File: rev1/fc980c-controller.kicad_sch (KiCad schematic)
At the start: 31 parts, among them J1 SWD, J2 USB, J3 KEYBOARD, SW1 BOOT0, U1 XC6206P332MR, U2 STM32F401CBUx, U3 USBLC6-2SC6, U5 PCA9306DC, Y1 8MHz C_l 20pF

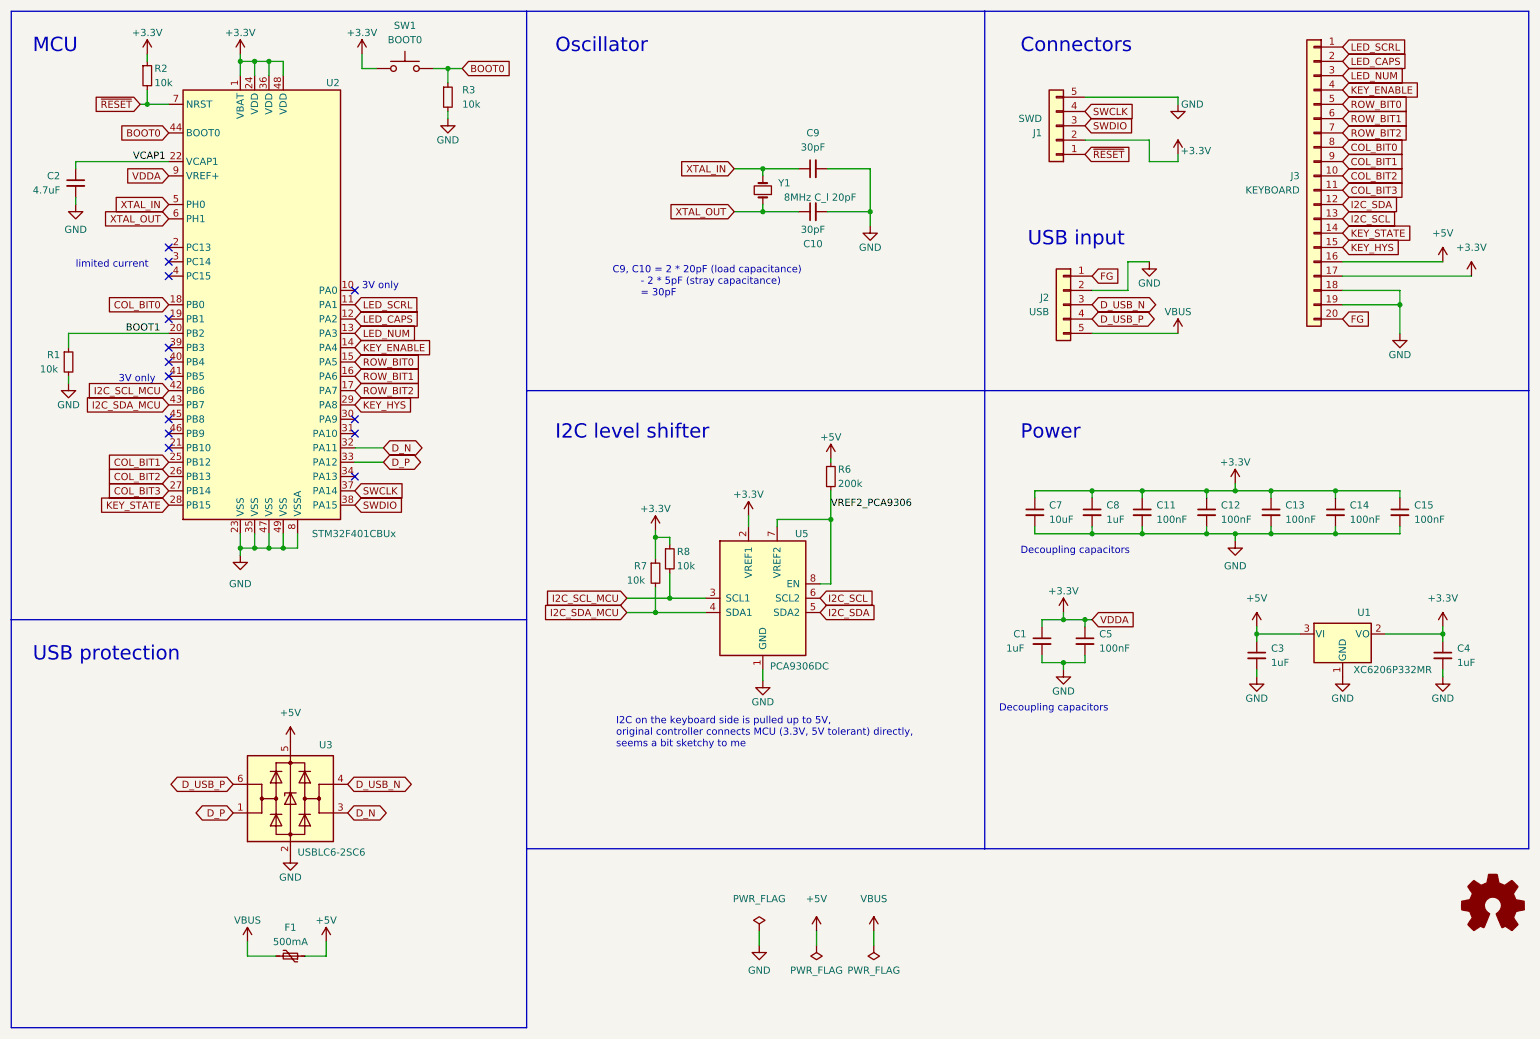
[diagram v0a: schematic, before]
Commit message: rev1: Add EEPROM
This should alleviate needing to use MCU flash for EEPROM emulation.

Also recalculate crystal load capacitor values using guidance from the
MCU datasheet.
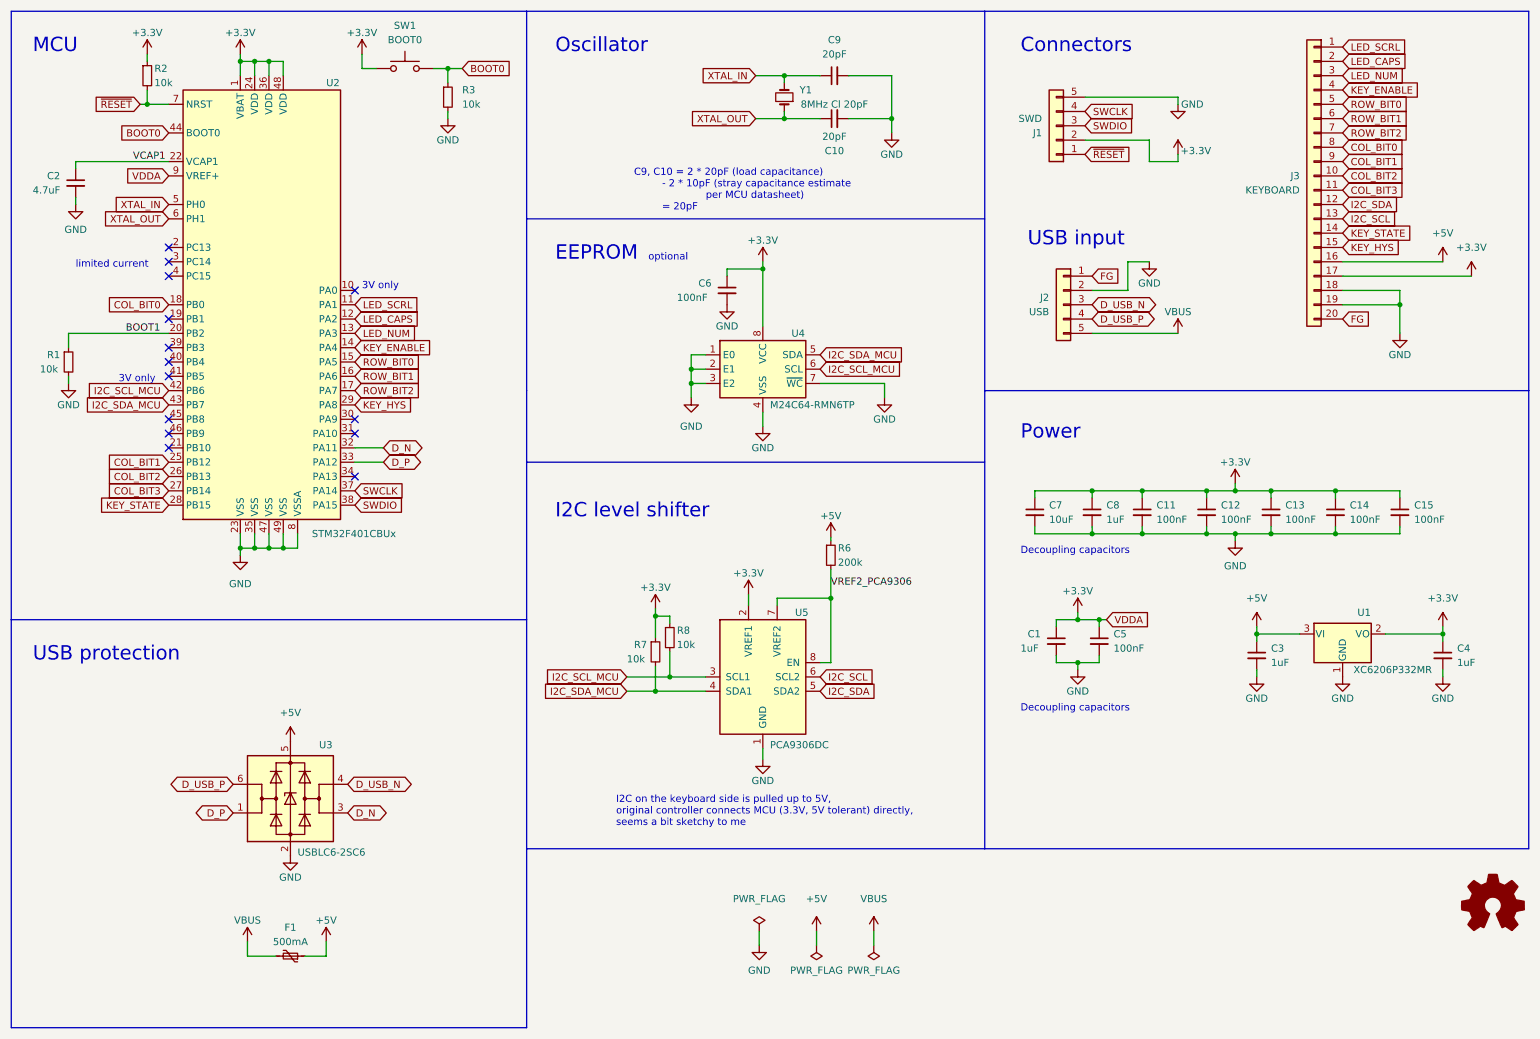
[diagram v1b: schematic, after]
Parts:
- added C6: 100nF, Resistor_SMD:R_0402_1005Metric, symbol Device:C_Small
- added U4: M24C64-RMN6TP, Package_SO:SOIC-8_3.9x4.9mm_P1.27mm, symbol Memory_EEPROM:M24C02-RMN
- C10, C9: value 30pF -> 20pF
- Y1: value 8MHz C_l 20pF -> 8MHz Cl 20pF
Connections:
- net +3.3V: now also C6.1, U4.8 (VCC)
- net GND: now also C6.2, U4.1 (E0), U4.2 (E1), U4.3 (E2), U4.4 (VSS), U4.7 (~{WC})
- net I2C_SCL_MCU: now also U4.6 (SCL)
- net I2C_SDA_MCU: now also U4.5 (SDA)
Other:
- note added: "C9, C10 = 2 * 20pF (load capacitance) - 2 * 10pF (stray capacitance estimate per MCU datasheet) = 20pF"
- note added: "EEPROM"
- note added: "optional"
- note removed: "C9, C10 = 2 * 20pF (load capacitance) - 2 * 5pF (stray capacitance) = 30pF"
- moved on the sheet: C1, C10, C5, C9, R6, R7, R8, U5, Y1

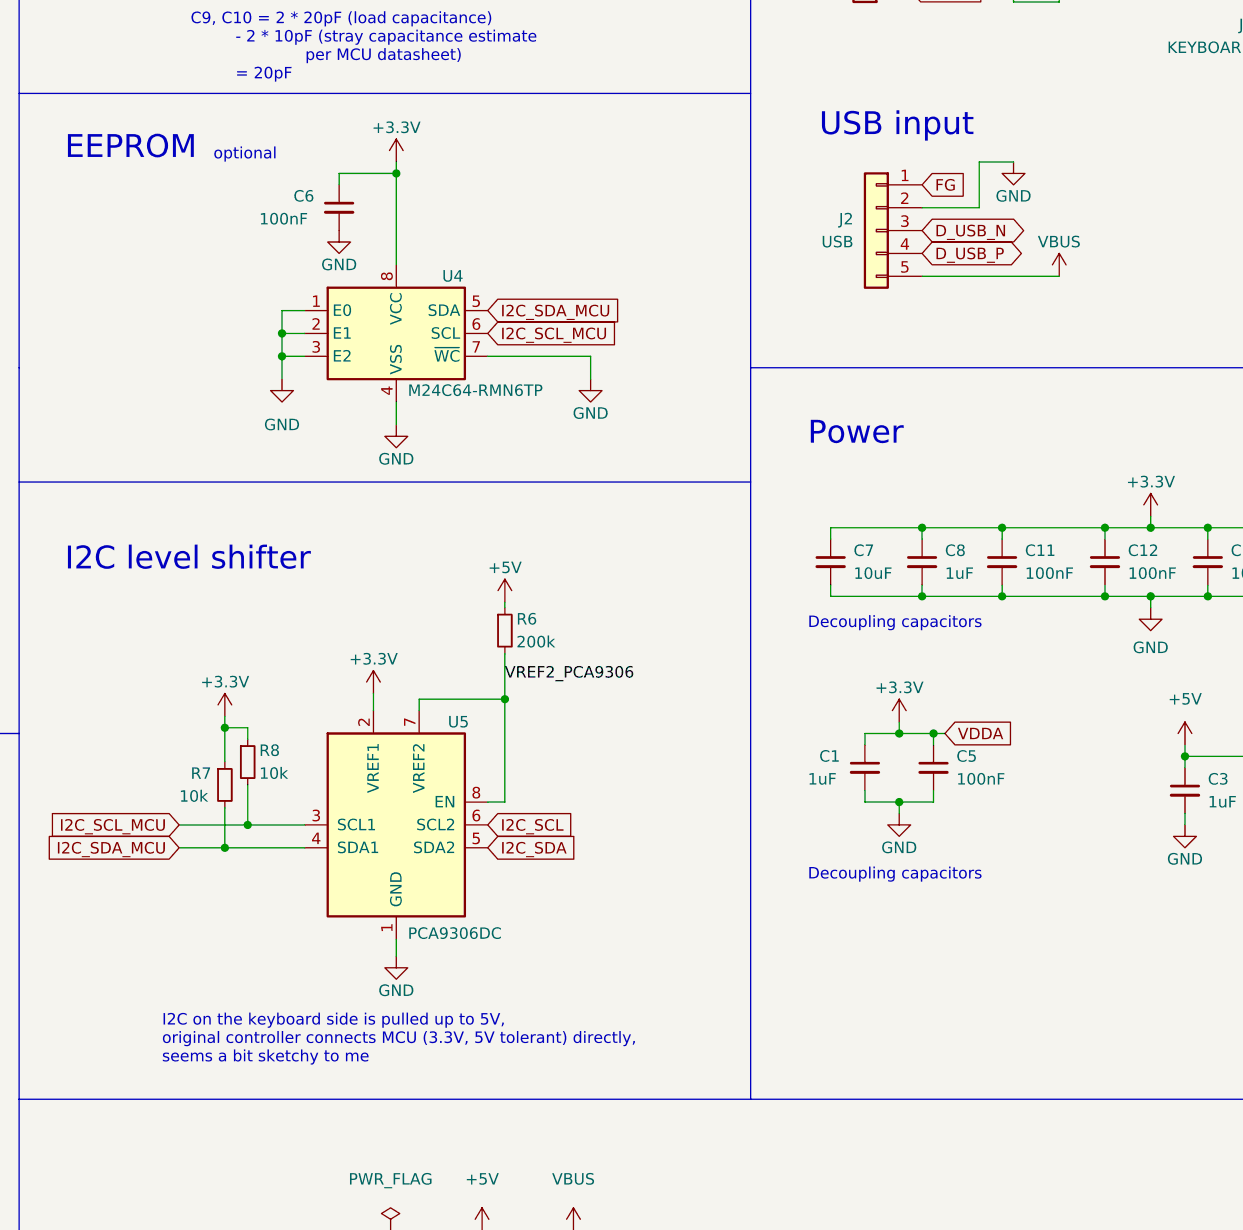
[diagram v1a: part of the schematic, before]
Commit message: rev1: Minor tweaks before first production run
Most notably change to a capacitor footprint rather than resistor
footprint for C6.

Small via tweaks.

Adjust component rotations reviewing JLC SMTA preview. (still waiting on
JLC review at this point)
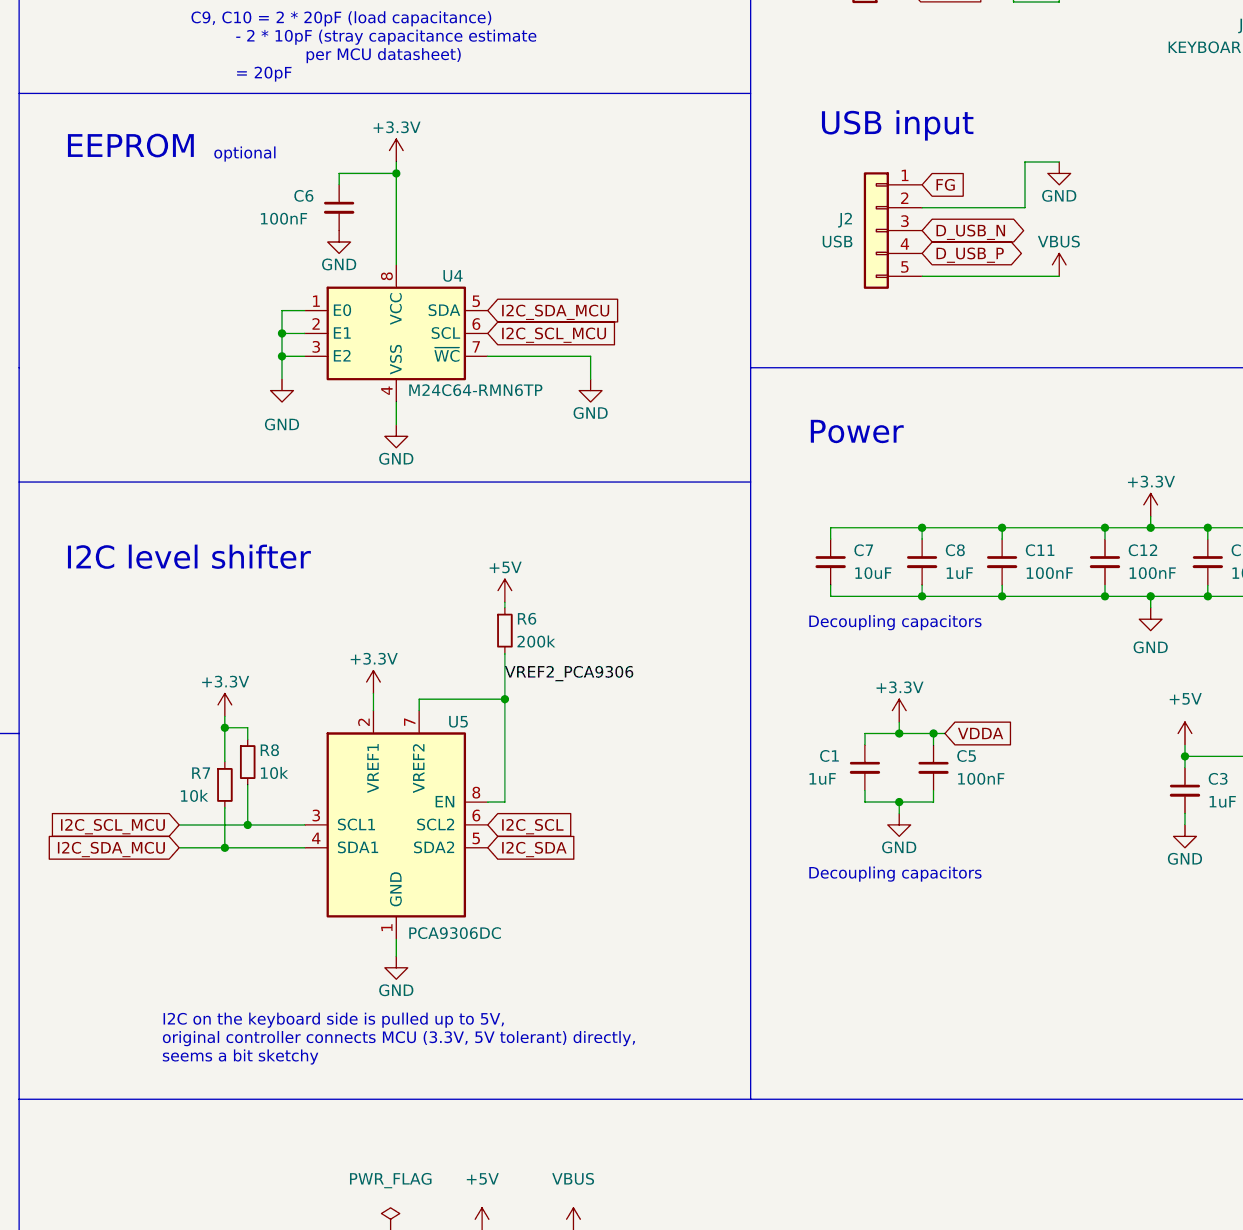
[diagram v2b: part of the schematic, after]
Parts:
- C6: footprint Resistor_SMD:R_0402_1005Metric -> Capacitor_SMD:C_0402_1005Metric
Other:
- note added: "I2C on the keyboard side is pulled up to 5V, original controller connects MCU (3.3V, 5V tolerant) directly, seems a bit sketchy"
- note removed: "I2C on the keyboard side is pulled up to 5V, original controller connects MCU (3.3V, 5V tolerant) directly, seems a bit sketchy to me"
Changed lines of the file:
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@@
     (stroke (width 0) (type default) (color 0 0 0 0))
   )
-  (wire (pts (xy 212.09 59.69) (xy 215.9 59.69))
+  (wire (pts (xy 217.17 59.69) (xy 220.98 59.69))
     (stroke (width 0) (type default) (color 0 0 0 0))
   )
@@
     (stroke (width 0) (type default) (color 0 0 0 0))
   )
-  (wire (pts (xy 205.74 64.77) (xy 212.09 64.77))
+  (wire (pts (xy 205.74 64.77) (xy 217.17 64.77))
     (stroke (width 0) (type default) (color 0 0 0 0))
   )
@@
     (stroke (width 0) (type default) (color 0 0 0 0))
   )
-  (wire (pts (xy 212.09 64.77) (xy 212.09 59.69))
+  (wire (pts (xy 217.17 64.77) (xy 217.17 59.69))
     (stroke (width 0) (type default) (color 0 0 0 0))
   )
@@
     (effects (font (size 2.54 2.54)) (justify left bottom))
   )
-  (text "I2C on the keyboard side is pulled up to 5V,\noriginal controller connects MCU (3.3V, 5V tolerant) directly,\nseems a bit sketchy to me\n"
+  (text "I2C on the keyboard side is pulled up to 5V,\noriginal controller connects MCU (3.3V, 5V tolerant) directly,\nseems a bit sketchy\n"
     (at 121.285 160.02 0)
     (effects (font (size 1.27 1.27)) (justify left bottom))
@@
       (effects (font (size 1.27 1.27)) (justify left))
     )
-    (property "Footprint" "Resistor_SMD:R_0402_1005Metric" (id 2) (at 140.97 64.77 0)
+    (property "Footprint" "Capacitor_SMD:C_0402_1005Metric" (id 2) (at 140.97 64.77 0)
       (effects (font (size 1.27 1.27)) hide)
     )
@@
     (pin "2")
   )
-  (symbol (lib_id "power:GND") (at 215.9 59.69 0) (unit 1)
-    (in_bom yes) (on_board yes)
-    (property "Reference" "#PWR017" (id 0) (at 215.9 66.04 0)
-      (effects (font (size 1.27 1.27)) hide)
-    )
-    (property "Value" "GND" (id 1) (at 215.9 63.5 0))
-    (property "Footprint" "" (id 2) (at 215.9 59.69 0)
-      (effects (font (size 1.27 1.27)) hide)
-    )
-    (property "Datasheet" "" (id 3) (at 215.9 59.69 0)
+  (symbol (lib_id "power:GND") (at 220.98 59.69 0) (unit 1)
+    (in_bom yes) (on_board yes)
+    (property "Reference" "#PWR017" (id 0) (at 220.98 66.04 0)
+      (effects (font (size 1.27 1.27)) hide)
+    )
+    (property "Value" "GND" (id 1) (at 220.98 63.5 0))
+    (property "Footprint" "" (id 2) (at 220.98 59.69 0)
+      (effects (font (size 1.27 1.27)) hide)
+    )
+    (property "Datasheet" "" (id 3) (at 220.98 59.69 0)
       (effects (font (size 1.27 1.27)) hide)
     )
@@
     )
     (path "/83d76cde-20a0-47d1-ab22-0b028dac3312"
-      (reference "C6") (unit 1) (value "100nF") (footprint "Resistor_SMD:R_0402_1005Metric")
+      (reference "C6") (unit 1) (value "100nF") (footprint "Capacitor_SMD:C_0402_1005Metric")
     )
     (path "/c1c939fb-fb05-4e5e-9033-217fdd266527"

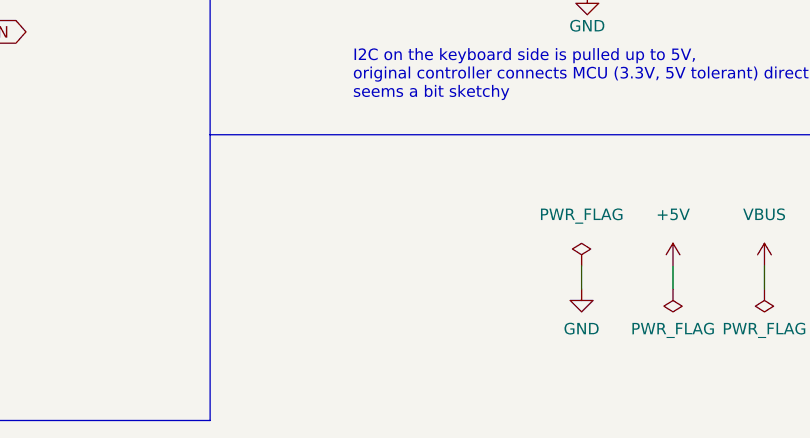
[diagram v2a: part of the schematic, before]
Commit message: rev1: Final production files for first run
Last tweak is to add tooling holes necessary for JLC PCB assembly. JLC
will place them on their own, however in their first attempt put one
hole over the silkscreen, so placing them manually should prevent this
in the future.
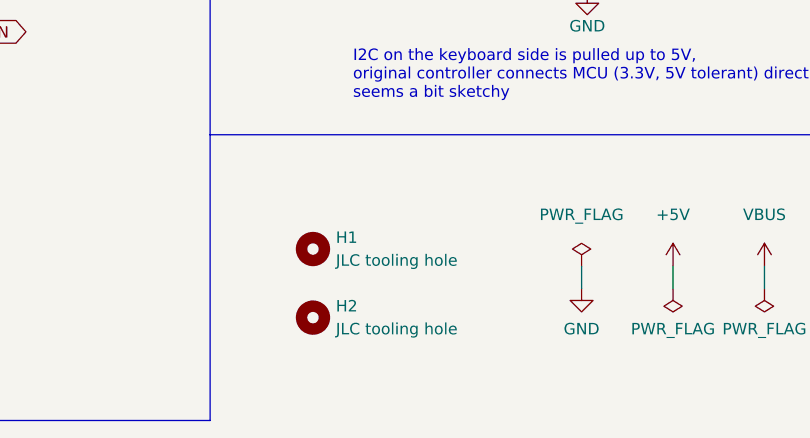
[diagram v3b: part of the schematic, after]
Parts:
- added H1, H2: JLC tooling hole, additional:JLC_tooling_hole, symbol Mechanical:MountingHole
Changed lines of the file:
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@@
     (pin "1")
+  )
+  (symbol (lib_id "Mechanical:MountingHole") (at 116.84 184.15 0) (unit 1)
+    (in_bom yes) (on_board yes) (fields_autoplaced)
+    (property "Reference" "H2" (id 0) (at 119.38 182.8799 0)
+      (effects (font (size 1.27 1.27)) (justify left))
+    )
+    (property "Value" "JLC tooling hole" (id 1) (at 119.38 185.4199 0)
+      (effects (font (size 1.27 1.27)) (justify left))
+    )
+    (property "Footprint" "additional:JLC_tooling_hole" (id 2) (at 116.84 184.15 0)
+      (effects (font (size 1.27 1.27)) hide)
+    )
+    (property "Datasheet" "~" (id 3) (at 116.84 184.15 0)
+      (effects (font (size 1.27 1.27)) hide)
+    )
   )
   (symbol (lib_id "power:+3.3V") (at 231.14 99.06 0) (unit 1)
@@
     (pin "1")
     (pin "2")
+  )
+  (symbol (lib_id "Mechanical:MountingHole") (at 116.84 176.53 0) (unit 1)
+    (in_bom yes) (on_board yes) (fields_autoplaced)
+    (property "Reference" "H1" (id 0) (at 119.38 175.2599 0)
+      (effects (font (size 1.27 1.27)) (justify left))
+    )
+    (property "Value" "JLC tooling hole" (id 1) (at 119.38 177.7999 0)
+      (effects (font (size 1.27 1.27)) (justify left))
+    )
+    (property "Footprint" "additional:JLC_tooling_hole" (id 2) (at 116.84 176.53 0)
+      (effects (font (size 1.27 1.27)) hide)
+    )
+    (property "Datasheet" "~" (id 3) (at 116.84 176.53 0)
+      (effects (font (size 1.27 1.27)) hide)
+    )
   )
   (symbol (lib_id "power:GND") (at 220.98 59.69 0) (unit 1)
@@
       (reference "F1") (unit 1) (value "500mA") (footprint "Fuse:Fuse_1206_3216Metric")
     )
+    (path "/85259554-ee62-4e2d-a196-3ac27664d817"
+      (reference "H1") (unit 1) (value "JLC tooling hole") (footprint "additional:JLC_tooling_hole")
+    )
+    (path "/455a3ebb-a602-4ffa-bcc4-bc22996e70a4"
+      (reference "H2") (unit 1) (value "JLC tooling hole") (footprint "additional:JLC_tooling_hole")
+    )
     (path "/694a0a3f-ee53-4373-9c1c-a41436b9e892"
